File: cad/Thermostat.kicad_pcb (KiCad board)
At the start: 2 copper layers, 119.4 x 50.8 mm, 24 parts, among them J1 Screw_Terminal_01x03, J3 Screw_Terminal_01x02, J4 Screw_Terminal_01x02, SW1 Rotary_Encoder_Switch, U1 WeMos_mini, U2 ILI9341_LCD_Breakout, U3 xl-007

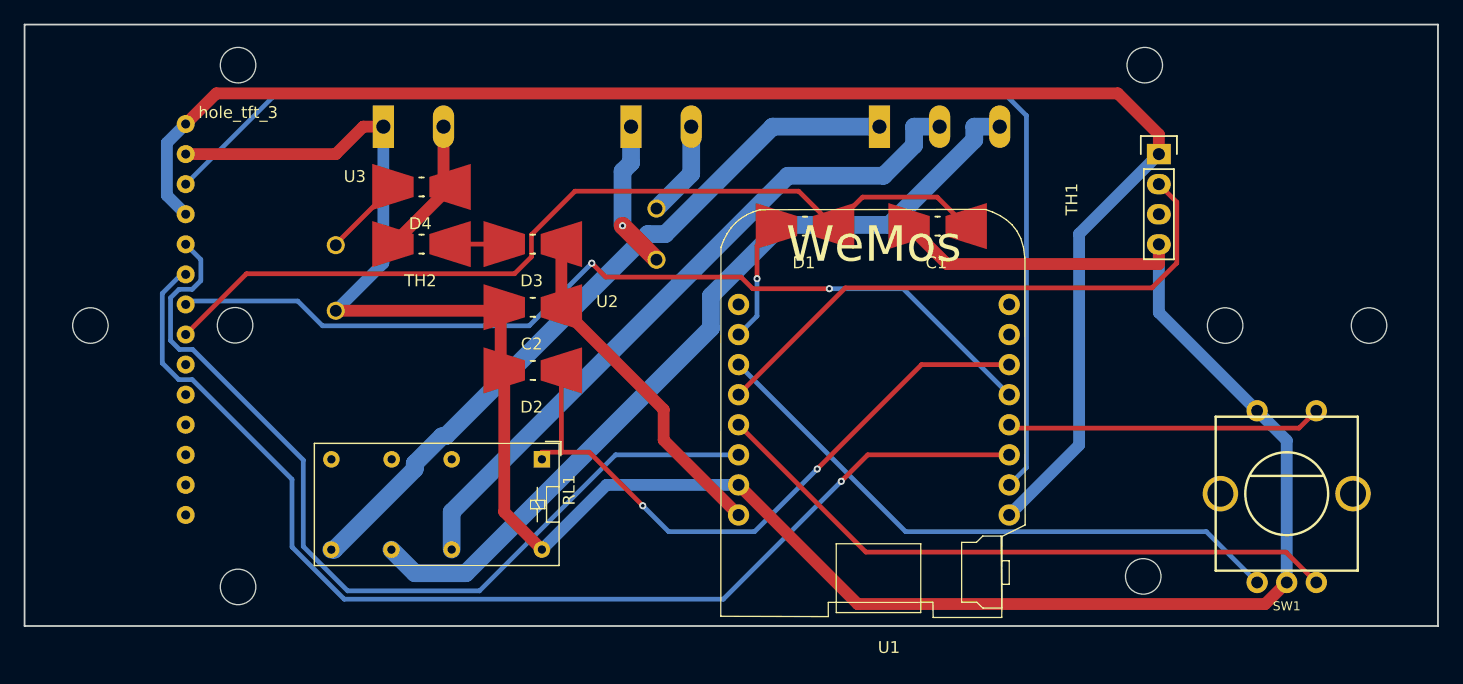
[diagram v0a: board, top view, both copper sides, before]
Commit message: correction for plastic box design
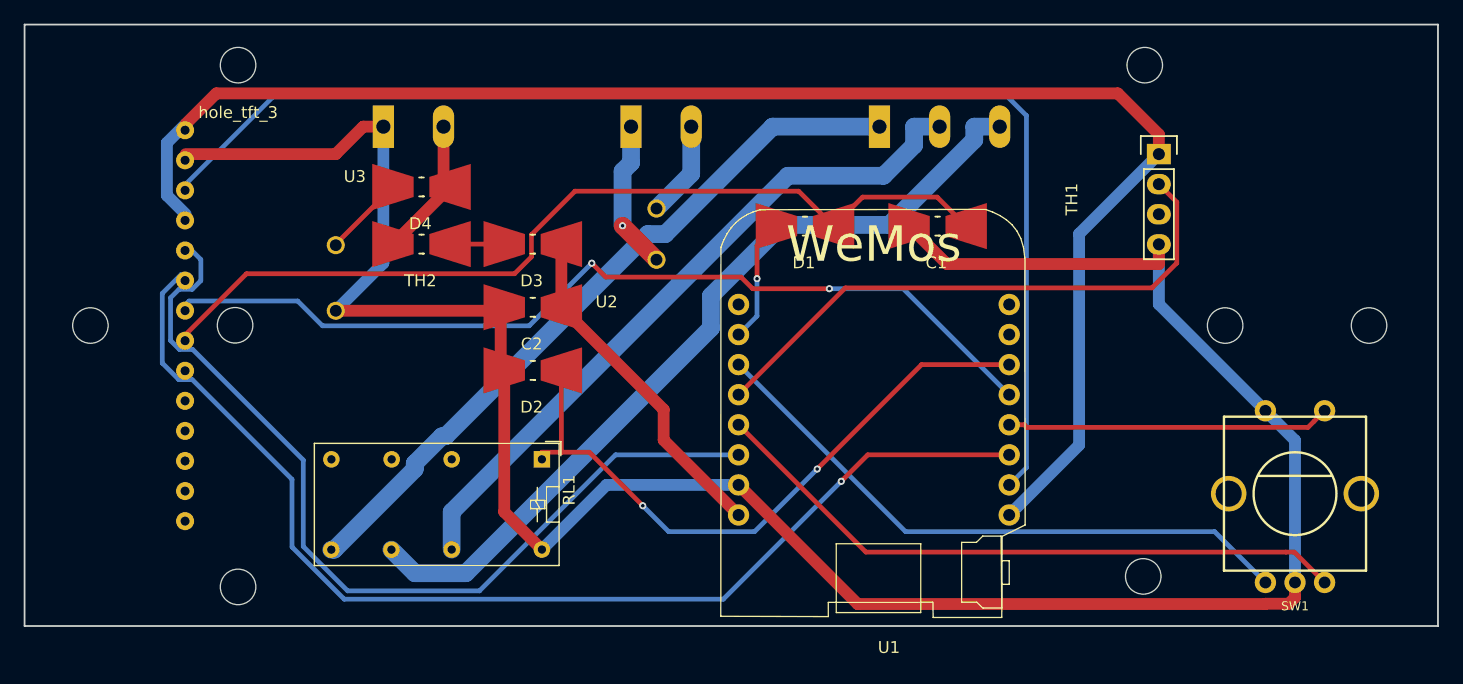
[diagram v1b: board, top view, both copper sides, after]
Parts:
- moved SW1 0.70 mm to (188.8, 84.6)
- moved U2 0.06 mm to (136.1, 70.4)
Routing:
- net GND: track 198.1 -> 199.8 mm
- net ENC_BUT: track 26.7 -> 27.7 mm
- net ENC_B: track 54.3 -> 55.0 mm
- net ENC_A: track 51.4 -> 52.1 mm
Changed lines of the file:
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@@
     (links 37)
     (no_connects 0)
-    (area 79.379714 43.065 204.45 99.365)
+    (area 79.379714 43.112 202.808286 98.945)
     (thickness 1.6)
     (drawings 6)
-    (tracks 160)
+    (tracks 167)
     (zones 0)
     (modules 24)
@@
   )
   (module sparkfun:SF-ROTARY-ENCODER (layer F.Cu)
-    (at 188.14 84.58)
+    (at 188.84 84.58)
     (fp_text reference SW1 (at 0 9.5) (layer F.SilkS)
       (effects (font (size 0.762 0.762) (thickness 0.1524)))
@@
   )
   (module "ILI9431:ILI9431 2,8 TFT" (layer F.Cu)
-    (at 136.144 70.358)
+    (at 136.09 70.38)
     (fp_text reference U2 (at -5.4 -2) (layer F.SilkS)
       (effects (font (size 1 1) (thickness 0.15)))
@@
     (fp_line (start 43 25) (end -43 25) (layer F.CrtYd) (width 0.15))
     (fp_line (start -43 25) (end -43 -25) (layer F.CrtYd) (width 0.15))
-    (pad 1 thru_hole circle (at -41 -17) (size 1.524 1.524) (drill 0.762) (layers *.Cu *.Mask)
+    (pad 1 thru_hole circle (at -41 -16.5) (size 1.524 1.524) (drill 0.762) (layers *.Cu *.Mask)
       (net 13 +3V3))
-    (pad 2 thru_hole circle (at -41 -14.46) (size 1.524 1.524) (drill 0.762) (layers *.Cu *.Mask)
-      (net 2 GND))
-    (pad 3 thru_hole circle (at -41 -11.92) (size 1.524 1.524) (drill 0.762) (layers *.Cu *.Mask)
+    (pad 2 thru_hole circle (at -41 -13.96) (size 1.524 1.524) (drill 0.762) (layers *.Cu *.Mask)
+      (net 2 GND))
+    (pad 3 thru_hole circle (at -41 -11.42) (size 1.524 1.524) (drill 0.762) (layers *.Cu *.Mask)
       (net 18 DISP_CS))
-    (pad 4 thru_hole circle (at -41 -9.38) (size 1.524 1.524) (drill 0.762) (layers *.Cu *.Mask)
+    (pad 4 thru_hole circle (at -41 -8.88) (size 1.524 1.524) (drill 0.762) (layers *.Cu *.Mask)
       (net 13 +3V3))
-    (pad 5 thru_hole circle (at -41 -6.84) (size 1.524 1.524) (drill 0.762) (layers *.Cu *.Mask)
+    (pad 5 thru_hole circle (at -41 -6.34) (size 1.524 1.524) (drill 0.762) (layers *.Cu *.Mask)
       (net 17 DISP_DC))
-    (pad 6 thru_hole circle (at -41 -4.3) (size 1.524 1.524) (drill 0.762) (layers *.Cu *.Mask)
+    (pad 6 thru_hole circle (at -41 -3.8) (size 1.524 1.524) (drill 0.762) (layers *.Cu *.Mask)
       (net 19 DISP_MOSI))
-    (pad 7 thru_hole circle (at -41 -1.76) (size 1.524 1.524) (drill 0.762) (layers *.Cu *.Mask)
+    (pad 7 thru_hole circle (at -41 -1.26) (size 1.524 1.524) (drill 0.762) (layers *.Cu *.Mask)
       (net 20 DISP_SCK))
-    (pad 8 thru_hole circle (at -41 0.78) (size 1.524 1.524) (drill 0.762) (layers *.Cu *.Mask)
+    (pad 8 thru_hole circle (at -41 1.28) (size 1.524 1.524) (drill 0.762) (layers *.Cu *.Mask)
       (net 1 "Net-(C1-Pad1)"))
-    (pad 9 thru_hole circle (at -41 3.32) (size 1.524 1.524) (drill 0.762) (layers *.Cu *.Mask)
+    (pad 9 thru_hole circle (at -41 3.82) (size 1.524 1.524) (drill 0.762) (layers *.Cu *.Mask)
       (net 23 "Net-(U2-Pad9)"))
-    (pad 10 thru_hole circle (at -41 5.86) (size 1.524 1.524) (drill 0.762) (layers *.Cu *.Mask)
+    (pad 10 thru_hole circle (at -41 6.36) (size 1.524 1.524) (drill 0.762) (layers *.Cu *.Mask)
       (net 24 "Net-(U2-Pad10)"))
-    (pad 11 thru_hole circle (at -41 8.4) (size 1.524 1.524) (drill 0.762) (layers *.Cu *.Mask)
+    (pad 11 thru_hole circle (at -41 8.9) (size 1.524 1.524) (drill 0.762) (layers *.Cu *.Mask)
       (net 25 "Net-(U2-Pad11)"))
-    (pad 12 thru_hole circle (at -41 10.94) (size 1.524 1.524) (drill 0.762) (layers *.Cu *.Mask)
+    (pad 12 thru_hole circle (at -41 11.44) (size 1.524 1.524) (drill 0.762) (layers *.Cu *.Mask)
       (net 26 "Net-(U2-Pad12)"))
-    (pad 13 thru_hole circle (at -41 13.48) (size 1.524 1.524) (drill 0.762) (layers *.Cu *.Mask)
+    (pad 13 thru_hole circle (at -41 13.98) (size 1.524 1.524) (drill 0.762) (layers *.Cu *.Mask)
       (net 27 "Net-(U2-Pad13)"))
-    (pad 14 thru_hole circle (at -41 16.02) (size 1.524 1.524) (drill 0.762) (layers *.Cu *.Mask))
+    (pad 14 thru_hole circle (at -41 16.52) (size 1.524 1.524) (drill 0.762) (layers *.Cu *.Mask))
   )
   (gr_line (start 200.914 95.758) (end 200.914 44.958) (layer Edge.Cuts) (width 0.15))
@@
   (segment (start 124.3472 64.5761) (end 124.3472 62.7118) (width 0.4) (layer F.Cu) (net 1))
   (segment (start 122.9188 66.0045) (end 124.3472 64.5761) (width 0.4) (layer F.Cu) (net 1))
-  (segment (start 100.2775 66.0045) (end 122.9188 66.0045) (width 0.4) (layer F.Cu) (net 1))
-  (segment (start 95.144 71.138) (end 100.2775 66.0045) (width 0.4) (layer F.Cu) (net 1))
   (segment (start 152.3169 59.5291) (end 149.866 61.98) (width 0.4) (layer F.Cu) (net 1))
   (segment (start 158.6151 59.5291) (end 152.3169 59.5291) (width 0.4) (layer F.Cu) (net 1))
   (segment (start 161.066 61.98) (end 158.6151 59.5291) (width 0.4) (layer F.Cu) (net 1))
+  (segment (start 100.2775 66.0045) (end 122.9188 66.0045) (width 0.4) (layer F.Cu) (net 1))
+  (segment (start 95.144 71.138) (end 100.2775 66.0045) (width 0.4) (layer F.Cu) (net 1))
+  (segment (start 188.312792 93.88) (end 186.34 93.88) (width 1) (layer F.Cu) (net 2))
+  (segment (start 186.34 93.88) (end 186.3173 93.9027) (width 1) (layer F.Cu) (net 2))
+  (segment (start 188.84 92.08) (end 188.84 93.352792) (width 1) (layer F.Cu) (net 2))
+  (segment (start 188.84 93.352792) (end 188.312792 93.88) (width 1) (layer F.Cu) (net 2))
+  (segment (start 186.34 77.58) (end 188.84 80.08) (width 1) (layer B.Cu) (net 2))
+  (segment (start 188.84 80.08) (end 188.84 92.08) (width 1) (layer B.Cu) (net 2))
+  (segment (start 177.34 63.52) (end 177.34 68.58) (width 1) (layer B.Cu) (net 2))
+  (segment (start 177.34 68.58) (end 186.34 77.58) (width 1) (layer B.Cu) (net 2))
   (segment (start 107.8217 55.898) (end 110.1397 53.58) (width 1) (layer F.Cu) (net 2))
   (segment (start 95.144 55.898) (end 107.8217 55.898) (width 1) (layer F.Cu) (net 2))
   (segment (start 111.84 53.58) (end 110.1397 53.58) (width 1) (layer F.Cu) (net 2))
-  (segment (start 188.14 80.08) (end 185.64 77.58) (width 1) (layer B.Cu) (net 2))
-  (segment (start 188.14 92.08) (end 188.14 80.08) (width 1) (layer B.Cu) (net 2))
-  (segment (start 177.34 69.28) (end 177.34 63.52) (width 1) (layer B.Cu) (net 2))
-  (segment (start 185.64 77.58) (end 177.34 69.28) (width 1) (layer B.Cu) (net 2))
   (segment (start 159.4439 65.1839) (end 177.34 65.1839) (width 1) (layer F.Cu) (net 2))
   (segment (start 156.24 61.98) (end 159.4439 65.1839) (width 1) (layer F.Cu) (net 2))
@@
   (segment (start 111.84 65.11) (end 107.818 69.132) (width 1) (layer B.Cu) (net 2))
   (segment (start 111.84 53.58) (end 111.84 65.11) (width 1) (layer B.Cu) (net 2))
-  (segment (start 186.3173 93.9027) (end 188.14 92.08) (width 1) (layer F.Cu) (net 2))
   (segment (start 151.9027 93.9027) (end 186.3173 93.9027) (width 1) (layer F.Cu) (net 2))
   (segment (start 141.84 83.84) (end 151.9027 93.9027) (width 1) (layer F.Cu) (net 2))
@@
   (segment (start 112.52 89.31) (end 114.5104 91.3004) (width 1.5) (layer B.Cu) (net 9))
   (segment (start 163.9 53.58) (end 161.7497 53.58) (width 1.5) (layer B.Cu) (net 9))
-  (segment (start 155.946 87.786) (end 141.84 73.68) (width 0.4) (layer B.Cu) (net 10))
-  (segment (start 181.346 87.786) (end 155.946 87.786) (width 0.4) (layer B.Cu) (net 10))
-  (segment (start 185.64 92.08) (end 181.346 87.786) (width 0.4) (layer B.Cu) (net 10))
-  (segment (start 188.0741 89.5141) (end 190.64 92.08) (width 0.4) (layer F.Cu) (net 11))
+  (segment (start 141.84 73.68) (end 155.946 87.786) (width 0.4) (layer B.Cu) (net 10))
+  (segment (start 182.046 87.786) (end 186.34 92.08) (width 0.4) (layer B.Cu) (net 10))
+  (segment (start 155.946 87.786) (end 182.046 87.786) (width 0.4) (layer B.Cu) (net 10))
+  (segment (start 191.34 92.08) (end 188.7741 89.5141) (width 0.4) (layer F.Cu) (net 11))
+  (segment (start 188.7741 89.5141) (end 188.0741 89.5141) (width 0.4) (layer F.Cu) (net 11))
   (segment (start 152.5941 89.5141) (end 188.0741 89.5141) (width 0.4) (layer F.Cu) (net 11))
   (segment (start 141.84 78.76) (end 152.5941 89.5141) (width 0.4) (layer F.Cu) (net 11))
+  (segment (start 164.7 78.76) (end 165.972792 78.76) (width 0.4) (layer F.Cu) (net 12))
+  (segment (start 165.972792 78.76) (end 166.192793 78.980001) (width 0.4) (layer F.Cu) (net 12))
+  (segment (start 166.192793 78.980001) (end 189.939999 78.980001) (width 0.4) (layer F.Cu) (net 12))
+  (segment (start 189.939999 78.980001) (end 190.440001 78.479999) (width 0.4) (layer F.Cu) (net 12))
+  (segment (start 190.440001 78.479999) (end 191.34 77.58) (width 0.4) (layer F.Cu) (net 12))
   (segment (start 164.9849 79.0449) (end 164.7 78.76) (width 0.4) (layer F.Cu) (net 12))
-  (segment (start 189.1751 79.0449) (end 164.9849 79.0449) (width 0.4) (layer F.Cu) (net 12))
-  (segment (start 190.64 77.58) (end 189.1751 79.0449) (width 0.4) (layer F.Cu) (net 12))
   (segment (start 93.5537 54.9483) (end 95.144 53.358) (width 1) (layer B.Cu) (net 13))
   (segment (start 93.5537 59.3877) (end 93.5537 54.9483) (width 1) (layer B.Cu) (net 13))
